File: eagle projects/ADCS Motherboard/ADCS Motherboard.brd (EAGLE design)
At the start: 91 x 91 mm, 142 parts, among them J1 HDR_10_EZFET_DEBUGGER, J11 CNC_3221-10-0300-00, J3 CNC_3221-10-0300-00, J5 CNC_3221-10-0300-00, J7 TE-1734829-3, Q1 PMV16XN, Q2 IRLML6246TRPBF, Q3 IRLML2246TRPBF, U1 MSP430F5529IPN, U10 TSV991AILT, U2 TSV991AILT, U3 ADS7841E_2K5, U4 TSV991AILT, U7 HMC1053, U9 BMX160, Y1 32.768kHz, Y2 CSTCR4M00G15L99, Y3 32.768kHz

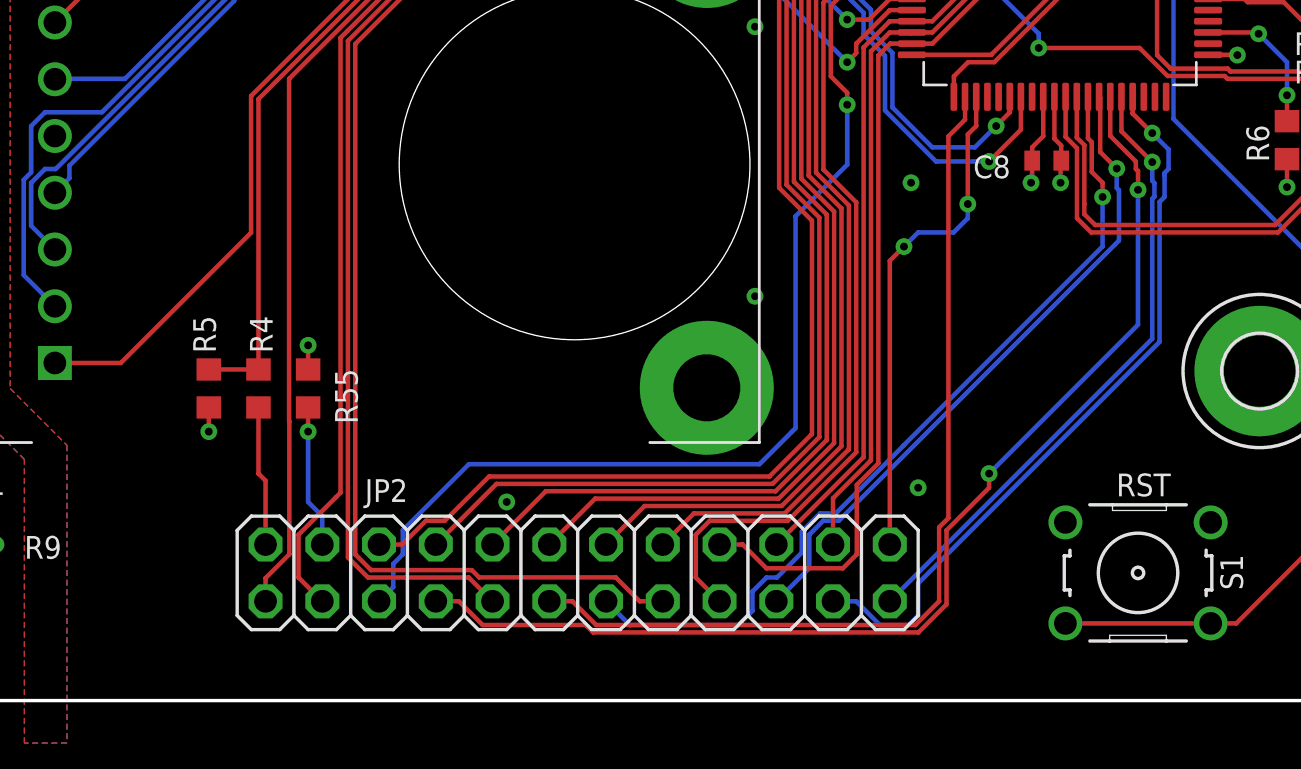
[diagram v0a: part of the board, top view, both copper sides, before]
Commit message: Added mobo-act brd mounting holes
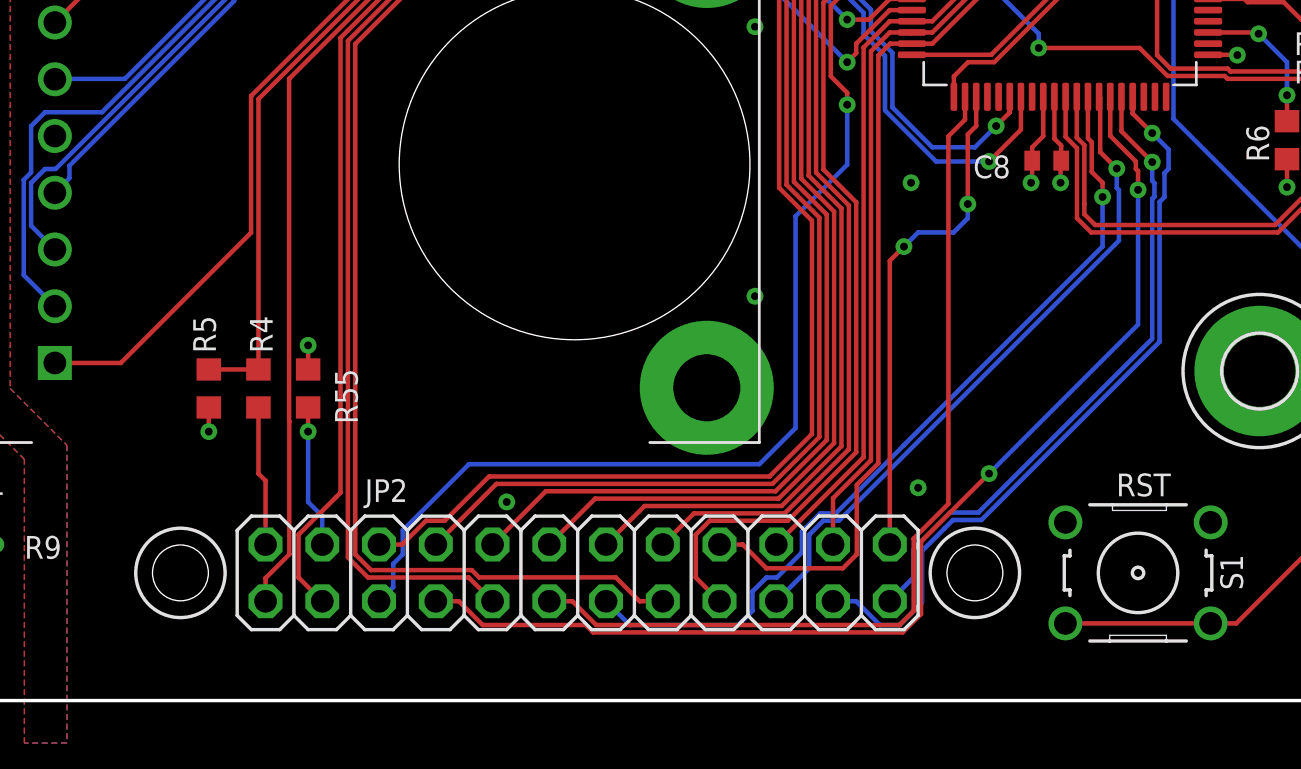
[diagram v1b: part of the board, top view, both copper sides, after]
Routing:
- net !CS!_CURR_SENSE_MTQR: track 28.1 -> 28.8 mm
- net !CS!_CURR_SENSE_RW: track 33.0 -> 33.5 mm
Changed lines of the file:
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@@
 <layer number="43" name="vRestrict" color="2" fill="10" visible="no" active="yes"/>
 <layer number="44" name="Drills" color="7" fill="1" visible="yes" active="yes"/>
-<layer number="45" name="Holes" color="7" fill="1" visible="no" active="yes"/>
+<layer number="45" name="Holes" color="7" fill="1" visible="yes" active="yes"/>
 <layer number="46" name="Milling" color="3" fill="1" visible="yes" active="yes"/>
 <layer number="47" name="Measures" color="7" fill="1" visible="yes" active="yes"/>
@@
 <rectangle x1="46.472475" y1="53.425725" x2="46.929675" y2="53.444775" layer="21"/>
 <rectangle x1="46.586775" y1="53.444775" x2="46.777275" y2="53.463825" layer="21"/>
+<hole x="27.94" y="5.715" drill="2.5"/>
+<circle x="27.94" y="5.715" radius="2" width="0.1524" layer="21"/>
+<hole x="63.5" y="5.715" drill="2.5"/>
+<circle x="63.5" y="5.715" radius="2" width="0.1524" layer="21"/>
 </plain>
 <attributes>
@@
 <wire x1="63.06" y1="27.025" x2="63.06" y2="26.001975" width="0.2032" layer="1"/>
 <contactref element="JP2" pad="11"/>
-<wire x1="62.3140125" y1="8.1709875" x2="61.8998" y2="7.756775" width="0.2032" layer="1"/>
-<wire x1="61.8998" y1="4.445" x2="61.8998" y2="7.756775" width="0.2032" layer="1"/>
 <wire x1="45.4858375" y1="4.445" x2="46.5494375" y2="3.3814" width="0.2032" layer="1"/>
 <wire x1="44.45" y1="4.445" x2="45.4858375" y2="4.445" width="0.2032" layer="1"/>
-<wire x1="46.5494375" y1="3.3814" x2="60.8362" y2="3.3814" width="0.2032" layer="1"/>
-<wire x1="60.8362" y1="3.3814" x2="61.8998" y2="4.445" width="0.2032" layer="1"/>
-<wire x1="62.3140125" y1="25.2559875" x2="62.3140125" y2="8.1709875" width="0.2032" layer="1"/>
+<wire x1="60.1305625" y1="3.3814" x2="46.5494375" y2="3.3814" width="0.2032" layer="1"/>
 <wire x1="63.06" y1="26.001975" x2="62.3140125" y2="25.2559875" width="0.2032" layer="1"/>
+<wire x1="60.75958125" y1="4.01041875" x2="60.1305625" y2="3.3814" width="0.2032" layer="1"/>
+<wire x1="62.3140125" y1="8.8059875" x2="60.75958125" y2="7.25155625" width="0.2032" layer="1"/>
+<wire x1="60.75958125" y1="7.25155625" x2="60.75958125" y2="4.01041875" width="0.2032" layer="1"/>
+<wire x1="62.3140125" y1="25.2559875" x2="62.3140125" y2="8.8059875" width="0.2032" layer="1"/>
 </signal>
 <signal name="RW_Z_DIR">
@@
 <wire x1="70.8025" y1="23.70085" x2="70.8025" y2="22.86" width="0.2032" layer="1"/>
 <via x="64.135" y="10.16" extent="1-16" drill="0.35"/>
-<wire x1="64.135" y1="10.16" x2="64.135" y2="9.525" width="0.2032" layer="1"/>
-<wire x1="64.135" y1="9.525" x2="62.23" y2="7.62" width="0.2032" layer="1"/>
 <wire x1="70.8025" y1="16.8275" x2="64.135" y2="10.16" width="0.2032" layer="16"/>
 <wire x1="70.8025" y1="22.86" x2="70.8025" y2="16.8275" width="0.2032" layer="16"/>
 <wire x1="69.56" y1="25.2737" x2="70.7037" y2="24.13" width="0.2032" layer="1"/>
 <wire x1="69.56" y1="27.025" x2="69.56" y2="25.2737" width="0.2032" layer="1"/>
-<wire x1="62.23" y1="4.308225" x2="60.972975" y2="3.0512" width="0.2032" layer="1"/>
-<wire x1="46.4126625" y1="3.0512" x2="60.972975" y2="3.0512" width="0.2032" layer="1"/>
-<wire x1="62.23" y1="7.62" x2="62.23" y2="4.308225" width="0.2032" layer="1"/>
 <wire x1="40.4058375" y1="4.445" x2="41.4694375" y2="3.3814" width="0.2032" layer="1"/>
 <wire x1="41.4694375" y1="3.3814" x2="46.0824625" y2="3.3814" width="0.2032" layer="1"/>
 <wire x1="46.0824625" y1="3.3814" x2="46.4126625" y2="3.0512" width="0.2032" layer="1"/>
+<wire x1="64.135" y1="10.16" x2="61.08978125" y2="7.11478125" width="0.2032" layer="1"/>
+<wire x1="61.08978125" y1="3.87364375" x2="61.08978125" y2="7.11478125" width="0.2032" layer="1"/>
+<wire x1="46.4126625" y1="3.0512" x2="60.2673375" y2="3.0512" width="0.2032" layer="1"/>
+<wire x1="60.2673375" y1="3.0512" x2="61.08978125" y2="3.87364375" width="0.2032" layer="1"/>
 </signal>
 <signal name="RW_Y_DIR">
@@
 <via x="71.4375" y="25.4" extent="1-16" drill="0.35"/>
 <wire x1="57.15" y1="4.445" x2="58.1858375" y2="4.445" width="0.2032" layer="16"/>
-<wire x1="60.5314" y1="3.3814" x2="59.2494375" y2="3.3814" width="0.2032" layer="16"/>
-<wire x1="58.1858375" y1="4.445" x2="59.2494375" y2="3.3814" width="0.2032" layer="16"/>
+<wire x1="59.25541875" y1="3.37541875" x2="58.1858375" y2="4.445" width="0.2032" layer="16"/>
 <wire x1="71.4375" y1="25.4" x2="70.56" y2="26.2775" width="0.2032" layer="1"/>
 <wire x1="70.56" y1="26.2775" x2="70.56" y2="27.025" width="0.2032" layer="1"/>
-<wire x1="60.96" y1="3.81" x2="60.5314" y2="3.3814" width="0.2032" layer="16"/>
 <wire x1="71.9884875" y1="23.6168375" x2="72.1713" y2="23.79965" width="0.2032" layer="16"/>
 <wire x1="72.1713" y1="23.79965" x2="72.1713" y2="24.6662" width="0.2032" layer="16"/>
 <wire x1="72.1713" y1="24.6662" x2="71.4375" y2="25.4" width="0.2032" layer="16"/>
 <wire x1="71.7677" y1="22.320475" x2="71.9884875" y2="22.5412625" width="0.2032" layer="16"/>
-<wire x1="71.9884875" y1="22.5412625" x2="71.9884875" y2="23.495" width="0.2032" layer="16"/>
-<wire x1="71.9884875" y1="23.495" x2="71.9884875" y2="23.6168375" width="0.2032" layer="16"/>
+<wire x1="71.9884875" y1="22.5412625" x2="71.9884875" y2="23.6168375" width="0.2032" layer="16"/>
 <wire x1="71.7677" y1="22.320475" x2="71.7677" y2="16.055725" width="0.2032" layer="16"/>
-<wire x1="71.7677" y1="16.055725" x2="60.96" y2="5.248025" width="0.2032" layer="16"/>
-<wire x1="60.96" y1="5.248025" x2="60.96" y2="3.81" width="0.2032" layer="16"/>
+<wire x1="60.1305625" y1="3.3814" x2="59.2614" y2="3.3814" width="0.2032" layer="16"/>
+<wire x1="59.2614" y1="3.3814" x2="59.25541875" y2="3.37541875" width="0.2032" layer="16"/>
+<wire x1="62.143353125" y1="7.706646875" x2="61.1324" y2="6.69569375" width="0.2032" layer="16"/>
+<wire x1="61.1324" y1="6.69569375" x2="61.1324" y2="4.3832375" width="0.2032" layer="16"/>
+<wire x1="61.1324" y1="4.3832375" x2="60.1305625" y2="3.3814" width="0.2032" layer="16"/>
+<wire x1="71.7677" y1="16.055725" x2="64.601975" y2="8.89" width="0.2032" layer="16"/>
+<wire x1="64.601975" y1="8.89" x2="63.794575" y2="8.0826" width="0.2032" layer="16"/>
+<wire x1="63.794575" y1="8.0826" x2="62.51930625" y2="8.0826" width="0.2032" layer="16"/>
+<wire x1="62.51930625" y1="8.0826" x2="62.143353125" y2="7.706646875" width="0.2032" layer="16"/>
 </signal>
 <signal name="!CS!_CURR_SENSE_MTQR">
@@
 <contactref element="U1" pad="56"/>
 <via x="71.4375" y="24.1036" extent="1-16" drill="0.35"/>
-<wire x1="71.4375" y1="16.1925" x2="59.69" y2="4.445" width="0.2032" layer="16"/>
 <wire x1="71.4375" y1="23.26275" x2="71.5363" y2="23.16395" width="0.2032" layer="16"/>
 <wire x1="71.5363" y1="23.16395" x2="71.5363" y2="22.55605" width="0.2032" layer="16"/>
@@
 <wire x1="71.4375" y1="24.1036" x2="70.06" y2="25.4811" width="0.2032" layer="1"/>
 <wire x1="70.06" y1="25.4811" x2="70.06" y2="27.025" width="0.2032" layer="1"/>
+<wire x1="60.7536" y1="5.5086" x2="59.69" y2="4.445" width="0.2032" layer="16"/>
+<wire x1="60.7536" y1="6.78386875" x2="60.7536" y2="5.5086" width="0.2032" layer="16"/>
+<wire x1="63.6578" y1="8.4128" x2="62.38253125" y2="8.4128" width="0.2032" layer="16"/>
+<wire x1="71.4375" y1="16.1925" x2="63.6578" y2="8.4128" width="0.2032" layer="16"/>
+<wire x1="62.38253125" y1="8.4128" x2="60.7536" y2="6.78386875" width="0.2032" layer="16"/>
 </signal>
 <signal name="N$4">

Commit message: Rev B almost ready
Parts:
- removed J3: CNC_3221-10-0300-00, my_library:CNC_3221-10-0300-00
- added JP1: (no value), pinhead:2X05
- moved C7 14.2 mm to (73.0, 44.5)
- moved Q1 14.2 mm to (73.0, 48.6)
- moved R36 14.2 mm to (73.0, 51.8)
- moved R7 14.2 mm to (73.0, 46.0)
- moved J5 9.85 mm to (84.8, 49.5)
- moved R45 5.41 mm to (80.3, 70.8)
- moved JP4 1.59 mm to (79.4, 45.4)
- moved R42 1.42 mm to (84.5, 36.2), turned to 180 degrees
- moved Y2 0.32 mm to (78.3, 35.2)
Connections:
- net !CS!_SUN_X+: now also JP1.2; no longer J3.2
- net !CS!_SUN_X-: now also JP1.7; no longer J3.7
- net !CS!_SUN_Y+: now also JP1.4; no longer J3.4
- net !CS!_SUN_Y-: now also JP1.9; no longer J3.9
- net !CS!_SUN_Z-: now also JP1.6; no longer J3.6
- net N$58: now also JP1.8; no longer J3.8
- net UCB0_SPI_CLK: now also JP1.5; no longer J3.5
- net UCB0_SPI_MISO: now also JP1.1; no longer J3.1
- net UCB0_SPI_MOSI: now also JP1.3; no longer J3.3
- net Z-_SUN_3V_PRESENT: now also JP1.10; no longer J3.10
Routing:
- net MSP_OBC_RESET: track 100.2 -> 86.6 mm
- net CAM_5V_PRESENT: track 93.1 -> 104.7 mm
- net CAMERA-2_SCL: track 78.4 -> 87.9 mm
- net UCB0_SPI_MOSI: track 127.0 -> 118.2 mm, vias 2 -> 1
- net !CS!_SUN_X+: track 45.1 -> 36.3 mm, vias 2 -> 1
- net RST/SBWTDIO: track 72.2 -> 63.8 mm
- net UCB0_SPI_MISO: track 124.4 -> 116.6 mm, vias 4 -> 3
- net UCB0_SPI_CLK: track 132.7 -> 126.1 mm, vias 2 -> 1
- net !CS!_SUN_Y+: track 39.7 -> 33.3 mm
- net N$58: track 8.27 -> 2.36 mm
- net CAMERA-1_SCL: track 94.0 -> 88.1 mm
- net !CS!_SUN_Z-: track 43.9 -> 38.5 mm
- net !CS!_SUN_X-: track 53.7 -> 48.5 mm
- net !CS!_SUN_Y-: track 46.9 -> 41.8 mm, vias 2 -> 1
- net CAMERA_SCLK: track 134.5 -> 130.0 mm
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
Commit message: Idk what i changed
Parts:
- Q1: value PMV16XN -> BSR802NL6327HTSA1
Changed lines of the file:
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@@
 <attribute name="SPICEPREFIX" value="R" x="73.025" y="51.7525" size="1.778" layer="27" display="off"/>
 </element>
-<element name="Q1" library="my_library" library_urn="urn:adsk.eagle:library:22876504" package="SOT23-3P95_230X110L20X43N_PMV16XN" package3d_urn="urn:adsk.eagle:package:24628515/1" value="PMV16XN" x="73.025" y="48.5775" smashed="yes" rot="R180">
+<element name="Q1" library="my_library" library_urn="urn:adsk.eagle:library:22876504" package="SOT23-3P95_230X110L20X43N_PMV16XN" package3d_urn="urn:adsk.eagle:package:24628515/1" value="BSR802NL6327HTSA1" x="73.025" y="48.5775" smashed="yes" rot="R180">
 <attribute name="NAME" x="71.12" y="48.895" size="1.016" layer="25" ratio="10" rot="R180"/>
 </element>
